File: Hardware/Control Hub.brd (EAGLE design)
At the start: 55.9 x 27.9 mm, 22 parts, among them IC1 LM555D, IC2 74AS08D, IC3 74AS08D

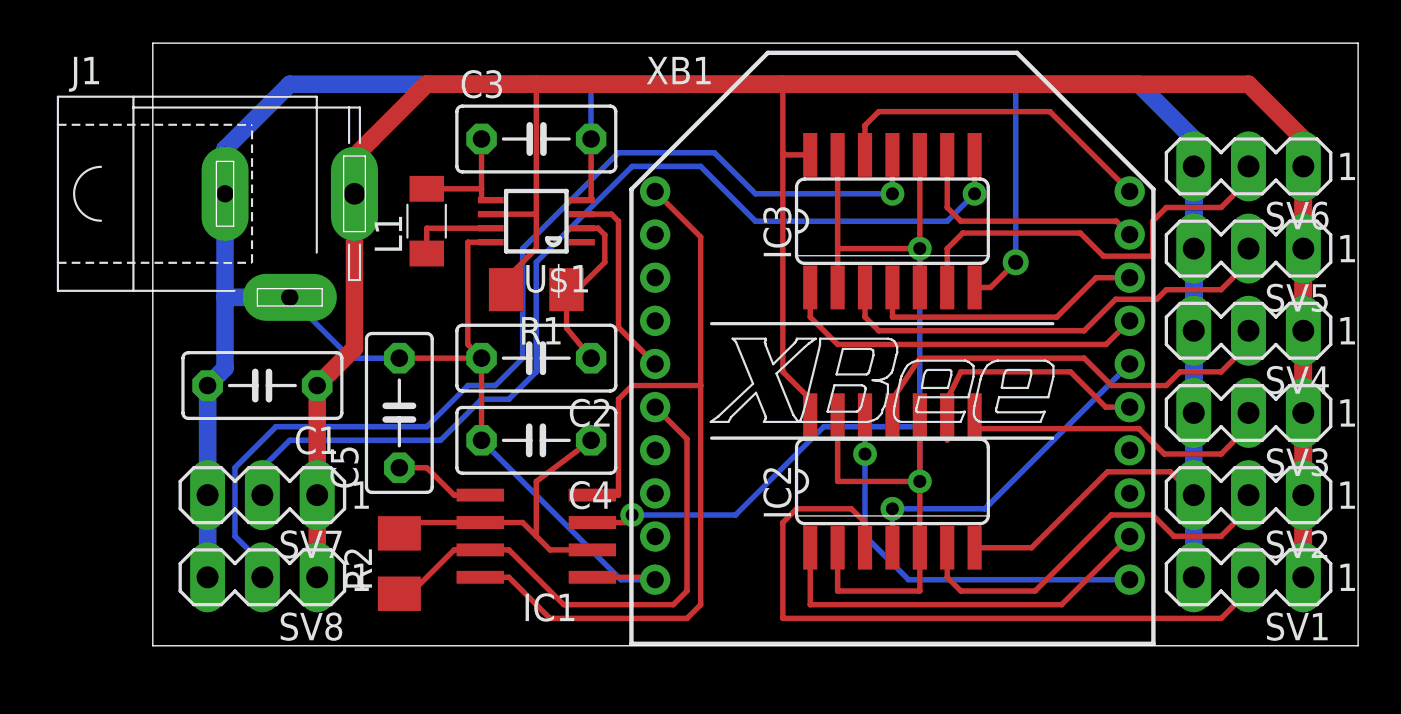
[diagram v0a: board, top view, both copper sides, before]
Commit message: Fixed board sizing and added logo
Added gitignore as well
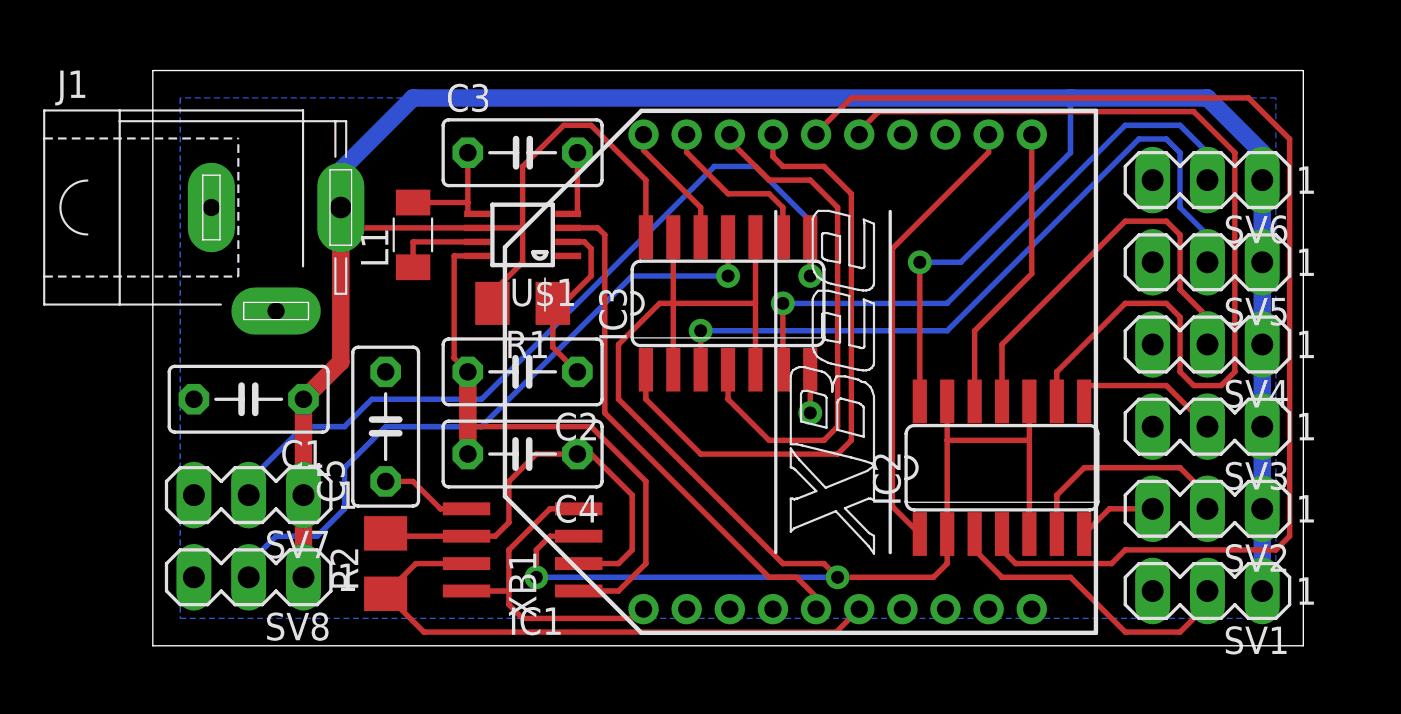
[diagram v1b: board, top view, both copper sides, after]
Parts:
- moved IC3 8.52 mm to (26.7, 15.9)
- moved IC2 5.12 mm to (39.4, 8.26)
- moved XB1 2.62 mm to (31.8, 12.7), turned to 90 degrees
- moved SV2 2.01 mm to (48.9, 6.35)
- moved SV6 2.01 mm to (48.9, 21.6)
- moved SV1 2.01 mm to (48.9, 2.54)
- moved SV3 2.01 mm to (48.9, 10.2)
- moved SV4 2.01 mm to (48.9, 14.0)
- moved SV5 2.01 mm to (48.9, 17.8)
- moved C2 0.90 mm to (17.1, 12.7)
- moved C3 0.90 mm to (17.1, 22.9)
- moved R1 0.90 mm to (17.1, 15.9)
- moved C4 0.90 mm to (17.1, 8.89)
- moved IC1 0.90 mm to (17.1, 4.45)
- moved C1 0.90 mm to (4.45, 11.4)
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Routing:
- net GND: track 164.9 -> 36.2 mm
- net N$16: track 15.6 -> 56.8 mm, vias 1 -> 0
- net N$15: track 11.8 -> 43.2 mm
- net +3V3: track 41.0 -> 15.2 mm
- net N$1: track 32.7 -> 14.3 mm
- net N$8: track 47.7 -> 31.3 mm
- net N$18: track 9.16 -> 24.0 mm
- net N$5: track 21.4 -> 33.6 mm, vias 0 -> 1
- net N$13: track 17.2 -> 29.0 mm
- net N$12: track 13.1 -> 24.2 mm
- net N$22: track 64.8 -> 75.8 mm, vias 3 -> 2
- net N$10: track 15.4 -> 5.85 mm
- net N$6: track 19.6 -> 28.0 mm, vias 0 -> 1
- net N$3: track 15.6 -> 7.24 mm
- net N$7: track 46.4 -> 38.1 mm
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- added copper zone on layer 16, net GND
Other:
- board size 55.9 x 27.9 mm -> 53.3 x 26.7 mm
- board text added: "Alex Crawford, 2012"
